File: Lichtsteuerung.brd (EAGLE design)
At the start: 157.7 x 86.4 mm, 155 parts, among them IC1 74HC595D, IC10 TSR_1-2450, IC11 MEGA64-A, IC12 75176AD, IC13 DS1307SO8, IC2 74HC595D, IC3 74HC595D, IC4 74HC595D, IC5 75176AD, IC6 MEGA8-AI, IC9 24FC128-I/SN, Q1 32.768, Q2 16MHz, Q3 16MHz, U1 MAX232SOIC16, X1 713-1410, X2 713-1410, X3 733-333, X5 713-1410, X6 733-334, X7 733-333, X8 733-333

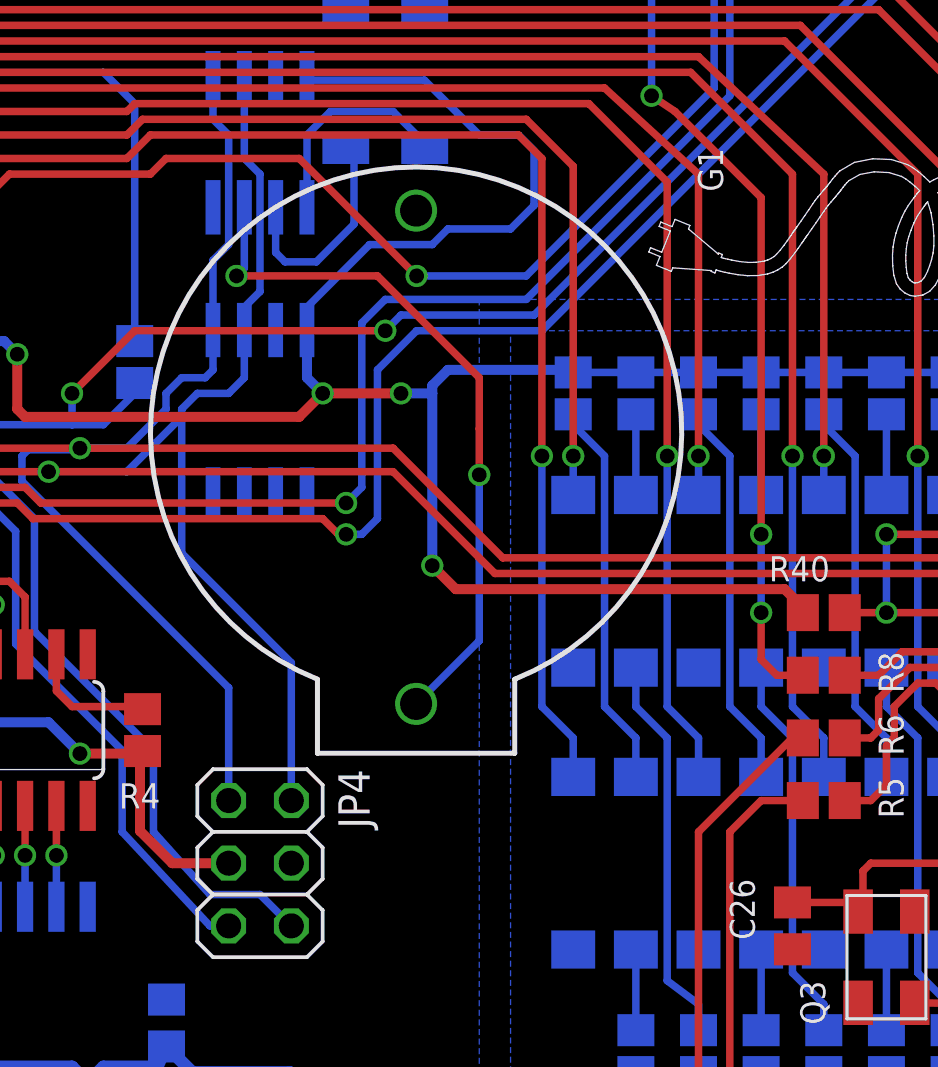
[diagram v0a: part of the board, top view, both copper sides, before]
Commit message: Changed CR2032 battery holder with a vertical one to allow easier replacements
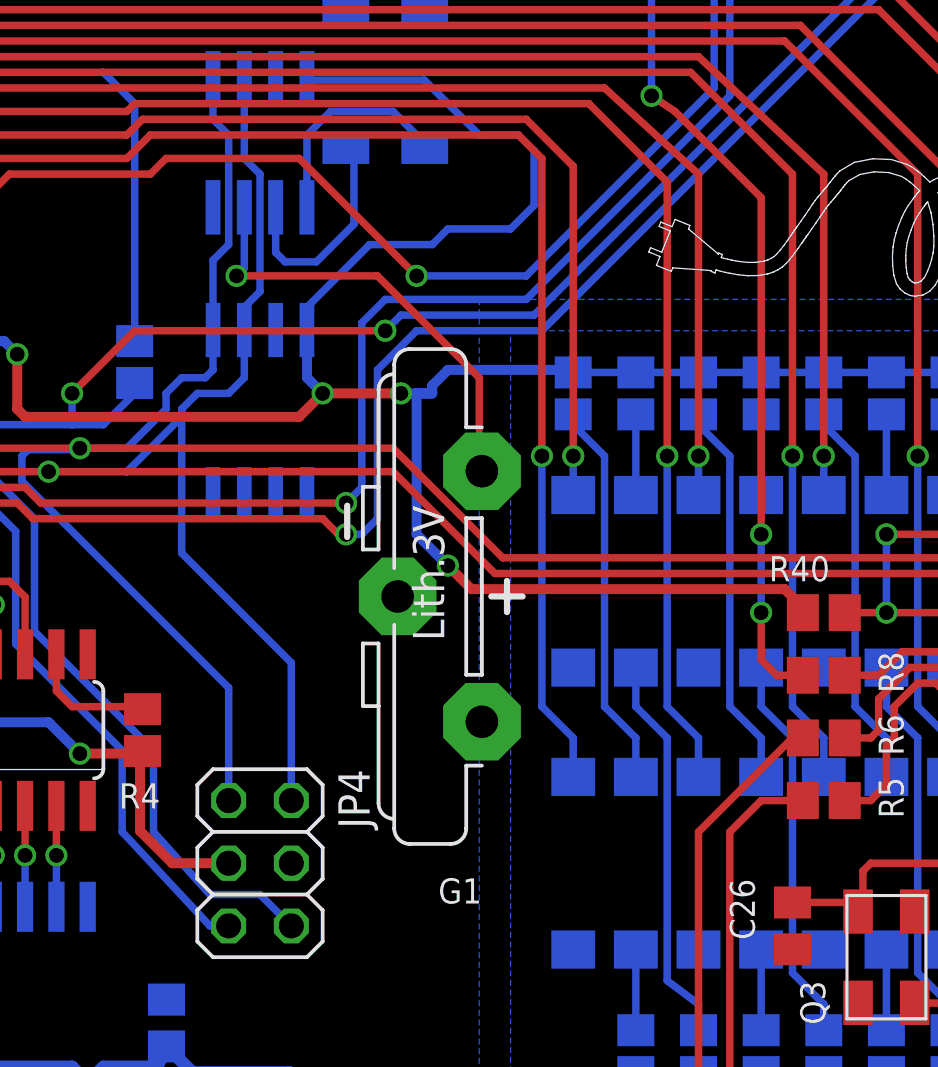
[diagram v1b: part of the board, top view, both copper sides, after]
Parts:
- G1: value (none) -> CR2032V; device SparkFun:BATTCOM_20MM_PTH -> cr2032v2:CR2032V2
- moved G1 15.6 mm to (104.2, 41.3), turned to 180 degrees
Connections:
- net GND: now also G1.-; no longer G1.2
- net N$40: now also G1.+; no longer G1.1
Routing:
- net N$40: track 28.8 -> 18.3 mm, vias 2 -> 1
- net +5V: track 543.3 -> 543.8 mm
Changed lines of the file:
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@@
 <setting verticaltext="up"/>
 </settings>
-<grid distance="50" unitdist="mil" unit="mil" style="lines" multiple="1" display="yes" altdistance="0.0125" altunitdist="inch" altunit="inch"/>
+<grid distance="0.000003125" unitdist="mm" unit="mm" style="lines" multiple="1" display="yes" altdistance="0.025" altunitdist="inch" altunit="inch"/>
 <layers>
 <layer number="1" name="Top" color="4" fill="1" visible="yes" active="yes"/>
@@
 <attribute name="NAME" x="95.25" y="61.2775" size="1.016" layer="26" rot="MR270"/>
 </element>
-<element name="G1" library="SparkFun" package="BATTCOM_20MM_PTH" value="" x="104.12" y="56.94" smashed="yes" rot="R270">
-<attribute name="NAME" x="115.55" y="59.48" size="1.016" layer="25" ratio="10" rot="R270"/>
+<element name="G1" library="cr2032v2" package="CR2032V2" value="CR2032V" x="104.2475" y="41.295" smashed="yes" rot="R180">
+<attribute name="NAME" x="106.7875" y="29.865" size="1.016" layer="25" ratio="10" rot="R180"/>
 </element>
 <element name="Q1" library="crystal" package="MC-306" value="32.768" x="102.87" y="62.23" smashed="yes" rot="MR90">
@@
 <contactref element="C9" pad="2"/>
 <contactref element="C10" pad="2"/>
-<contactref element="G1" pad="2"/>
+<contactref element="G1" pad="-"/>
 <contactref element="IC13" pad="4"/>
 <contactref element="C12" pad="2"/>
@@
 <wire x1="119.8" y1="40.64" x2="119.8" y2="40.855" width="0.4064" layer="1"/>
 <wire x1="119.8" y1="40.855" x2="119.0625" y2="41.5925" width="0.4064" layer="1"/>
-<wire x1="119.0625" y1="41.5925" x2="105.7275" y2="41.5925" width="0.4064" layer="1"/>
-<wire x1="105.7275" y1="41.5925" x2="104.775" y2="42.545" width="0.4064" layer="1"/>
-<via x="104.775" y="42.545" extent="1-16" drill="0.6"/>
-<wire x1="104.775" y1="42.545" x2="104.775" y2="49.53" width="0.4064" layer="16"/>
+<wire x1="119.0625" y1="41.5925" x2="106.3625" y2="41.5925" width="0.4064" layer="1"/>
+<wire x1="106.3625" y1="41.5925" x2="105.41" y2="42.545" width="0.4064" layer="1"/>
+<via x="105.41" y="42.545" extent="1-16" drill="0.6"/>
+<wire x1="105.41" y1="42.545" x2="104.14" y2="43.815" width="0.4064" layer="16"/>
+<wire x1="104.14" y1="43.815" x2="104.14" y2="49.53" width="0.4064" layer="16"/>
+<wire x1="104.14" y1="49.53" x2="104.775" y2="49.53" width="0.4064" layer="16"/>
 <wire x1="104.775" y1="49.53" x2="104.775" y2="49.8475" width="0.4064" layer="16"/>
 <wire x1="104.775" y1="49.8475" x2="105.41" y2="50.4825" width="0.4064" layer="16"/>
@@
 </signal>
 <signal name="N$40">
-<contactref element="G1" pad="1"/>
+<contactref element="G1" pad="+"/>
 <contactref element="IC13" pad="3"/>
 <wire x1="97.155" y1="57.0738" x2="97.155" y2="54.61" width="0.3048" layer="16"/>
@@
 <wire x1="102.5525" y1="54.2925" x2="106.68" y2="50.165" width="0.3048" layer="1"/>
 <wire x1="106.68" y1="50.165" x2="106.68" y2="48.095" width="0.3048" layer="1"/>
-<wire x1="106.68" y1="48.095" x2="106.68" y2="46.228" width="0.3048" layer="1"/>
-<via x="106.68" y="46.228" extent="1-16" drill="0.6" shape="square"/>
-<wire x1="106.68" y1="46.228" x2="106.68" y2="39.5" width="0.3048" layer="16"/>
-<wire x1="106.68" y1="39.5" x2="104.12" y2="36.94" width="0.3048" layer="16"/>
+<wire x1="106.68" y1="48.095" x2="106.68" y2="46.4825" width="0.254" layer="1"/>
+<wire x1="106.68" y1="46.4825" x2="106.7875" y2="46.375" width="0.254" layer="1"/>
 </signal>
 <signal name="SCL">

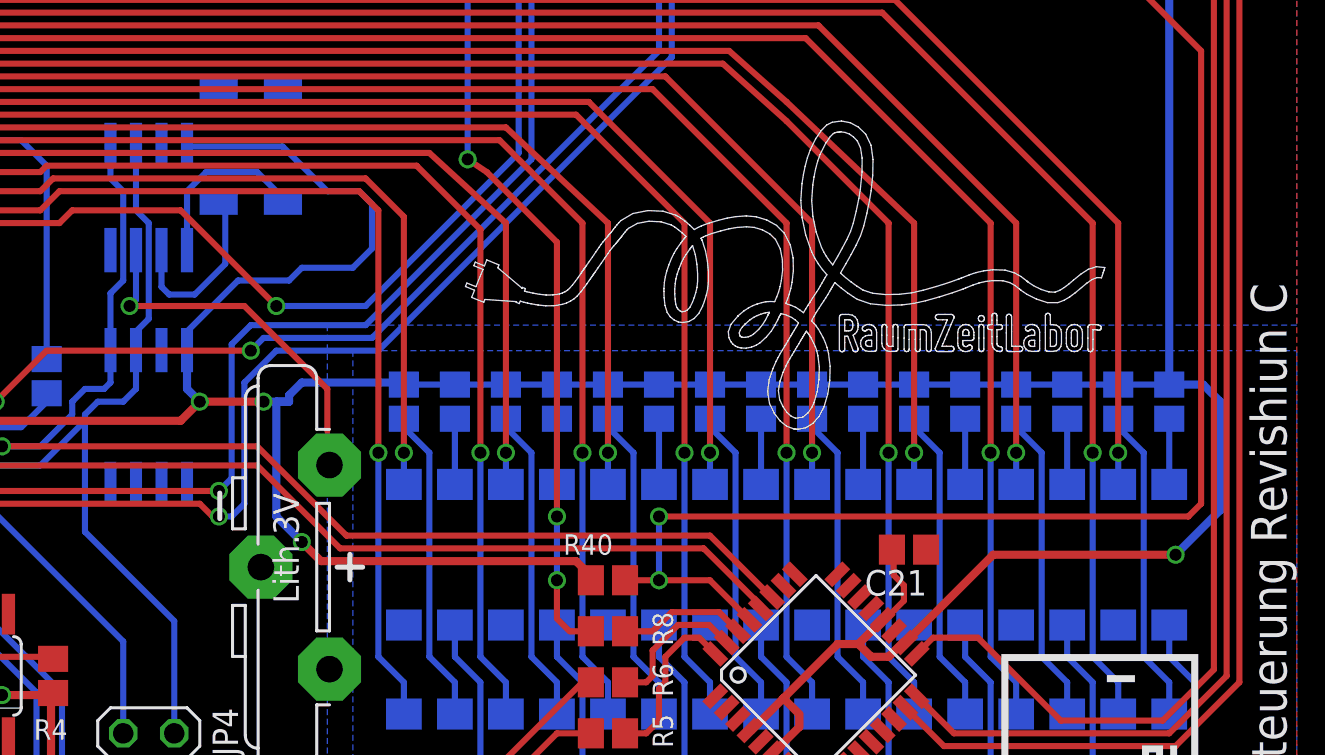
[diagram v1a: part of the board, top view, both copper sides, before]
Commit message: Added missing pulldowns for the optocoupler inputs
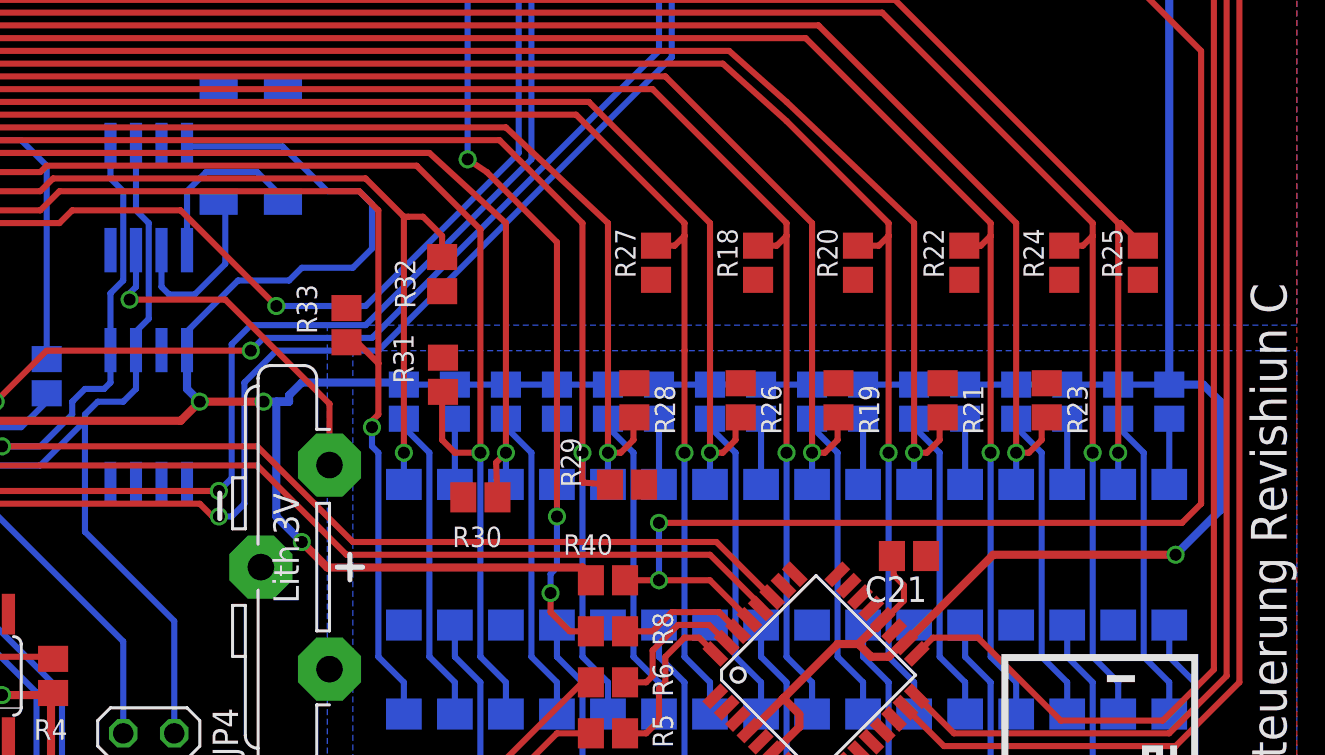
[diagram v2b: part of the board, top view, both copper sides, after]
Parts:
- removed U$1: (no value), RaumZeitLabor:RAUMZEITLABOR_-_LOGO_-_SCHWARZ
- added R18, R19, R20, R21, R22, R23, R24, R25, R26, R27, R28, R29, R30, R31, R32, R33: 10k, resistor:R0805
- moved C21 0.32 mm to (135.6, 41.8)
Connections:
- net GND: now also R18.1, R19.1, R20.1, R21.1, R22.1, R23.1, R24.1, R25.1, R26.1, R27.1, R28.1, R29.1, R30.1, R31.1, R32.1, R33.1
- net INPUT_1: now also R33.2
- net INPUT_10: now also R19.2
- net INPUT_11: now also R20.2
- net INPUT_12: now also R21.2
- net INPUT_13: now also R22.2
- net INPUT_14: now also R23.2
- net INPUT_15: now also R24.2
- net INPUT_16: now also R25.2
- net INPUT_2: now also R32.2
- net INPUT_3: now also R31.2
- net INPUT_4: now also R30.2
- net INPUT_5: now also R29.2
- net INPUT_6: now also R28.2
- net INPUT_7: now also R27.2
- net INPUT_8: now also R26.2
- net INPUT_9: now also R18.2
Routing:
- net INPUT_3: track 65.8 -> 70.4 mm
- net INPUT_2: track 49.9 -> 53.3 mm
- net INPUT_5: track 77.9 -> 80.8 mm
- net INPUT_8: track 79.5 -> 82.3 mm
- net INPUT_14: track 108.2 -> 111.0 mm
- net INPUT_12: track 106.1 -> 108.8 mm
- net INPUT_6: track 69.5 -> 72.2 mm
- net INPUT_10: track 105.2 -> 107.8 mm
- net INPUT_4: track 59.7 -> 62.2 mm
- net INPUT_1: track 60.2 -> 62.5 mm
- net INPUT_11: track 118.7 -> 120.4 mm
- net INPUT_16: track 110.2 -> 111.9 mm
- net INPUT_7: track 87.8 -> 89.4 mm
- net INPUT_15: track 122.4 -> 124.0 mm
- net INPUT_9: track 118.0 -> 119.7 mm
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
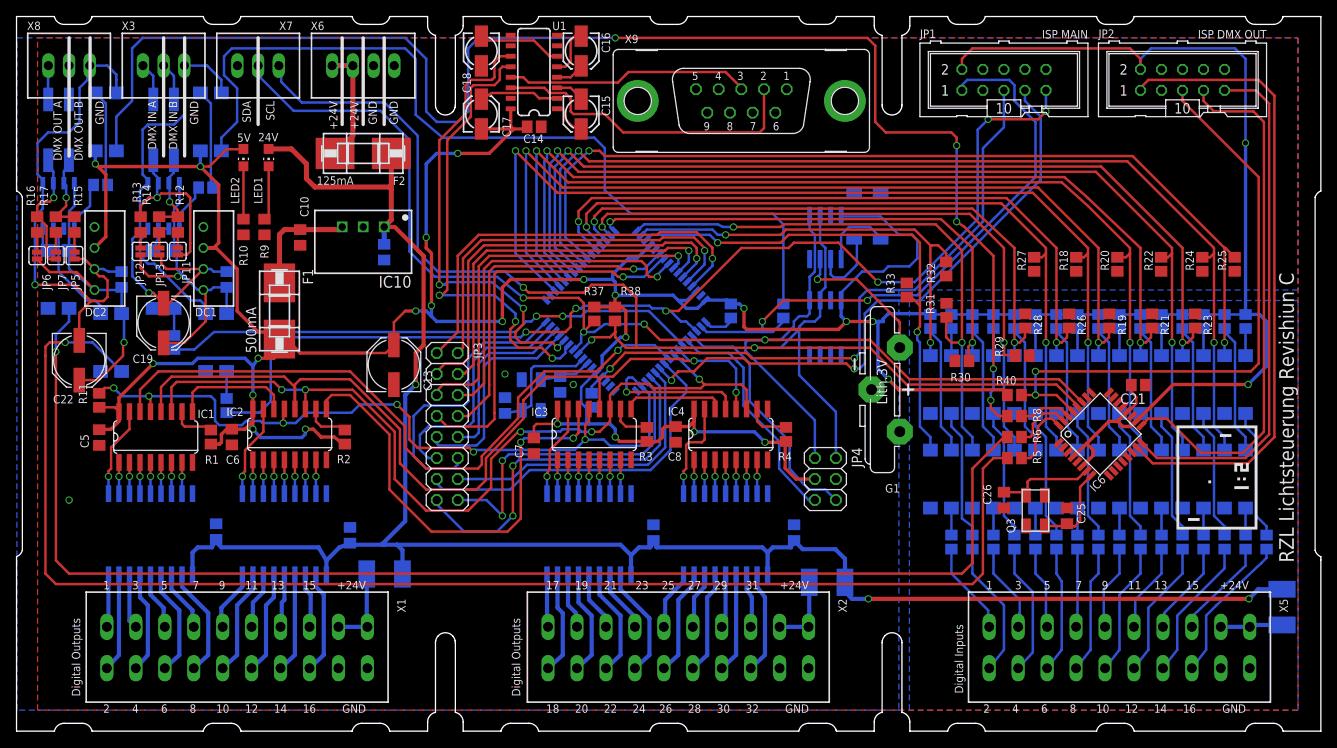
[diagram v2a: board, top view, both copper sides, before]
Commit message: Added new high-speed optocouplers
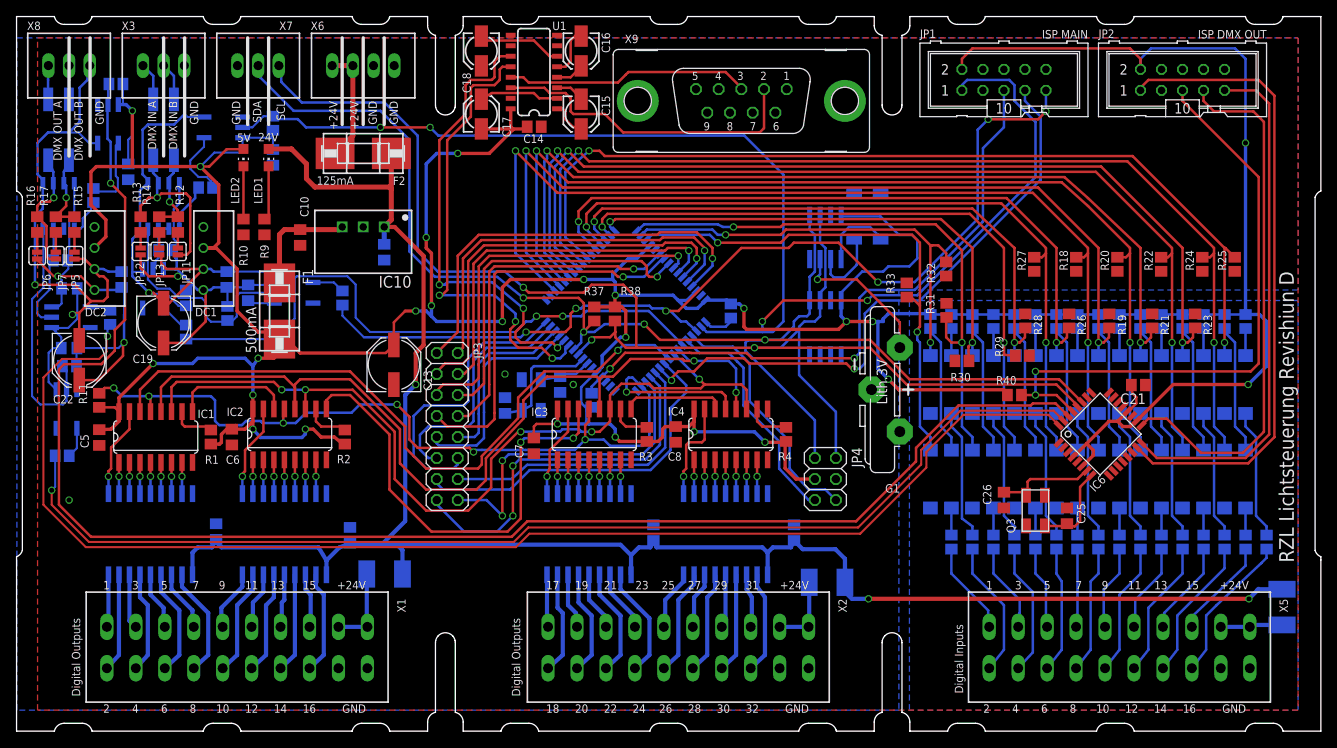
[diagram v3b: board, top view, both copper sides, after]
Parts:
- removed OK17, OK18, OK19, OK20, OK21, OK22: LTV356T, optocoupler:SMD4
- removed R5, R6: 220, resistor:R0805
- removed R76, R8: 10k, resistor:R0805
- added C24, C27, C28, C29, C30, C31: 100n, rcl:C0805
- added OK1, OK2, OK3, OK30, OK31, OK32: ACPL-M50L, ACPL-M50L:JEDEC_MS-012-AA_SOIC5
- added R34, R35, R36, R43, R44, R45: 1k, resistor:R0805
- added R41, R42: 220, resistor:R0805
- moved R74 19.1 mm to (39.4, 52.4)
- moved R7 16.0 mm to (11.3, 50.0), turned to 90 degrees
- moved R73 1.92 mm to (20.5, 48.2)
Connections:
- removed net N$106: OK17.3, R76.2
- removed net N$46: OK22.3, R8.2
- removed net N$47: OK20.1, R6.2
- removed net N$48: OK21.1, R5.2
- removed net REC$2: IC5.1, R7.2
- removed net RE_OUT1: IC5.2, IC5.3, OK21.3
- removed net TXD_OUT1: IC5.4, OK20.3
- new net N$73: OK2.1, R41.2
- new net N$79: OK1.1, R7.2
- new net REC$3: IC5.1, R42.2
- new net RE_OUT2: IC5.2, IC5.3, OK1.5, R43.1
- new net TXD_OUT2: IC5.4, OK2.5, R44.1
- net +5V: now also C30.1, C31.1, OK3.6, OK30.6, R36.1, R45.1; no longer OK17.4, OK22.4
- net DMX_O_D: now also R41.1; no longer R6.1
- net DMX_O_R: now also OK3.5, R45.2; no longer R8.1
- net GND: now also C30.2, C31.2, OK1.3, OK2.3, OK3.4, OK30.4, OK31.3, OK32.3; no longer OK18.2, OK19.2, OK20.2, OK21.2
- net GNDI1: now also C24.2, C27.2, OK30.3, OK31.4, OK32.4; no longer OK17.2
- net GNDI2: now also C28.2, C29.2, OK1.4, OK2.4, OK3.3; no longer OK22.2
- net N$104: now also OK30.1; no longer OK17.1
- net N$116: now also OK31.1; no longer OK18.1
- net N$133: now also OK32.1; no longer OK19.1
- net N$45: now also OK3.1, R42.1; no longer OK22.1, R7.1
- net RE/DE2: now also R7.1; no longer R5.1
- net RE_OUT: now also OK32.5, R34.1; no longer OK19.3
- net RXD/MOSI: now also OK30.5, R36.2; no longer R76.1
- net TXD_OUT: now also OK31.5, R35.1; no longer OK18.3
- net VCCIO1: now also C24.1, C27.1, OK31.6, OK32.6, R34.2, R35.2; no longer OK18.4, OK19.4
- net VCCIO2: now also C28.1, C29.1, OK1.6, OK2.6, R43.2, R44.2; no longer OK20.4, OK21.4
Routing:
- net DMX_O_R: track 6.55 -> 189.7 mm, vias 0 -> 1
- net N$46: track 177.6 -> 0.00 mm, vias 5 -> 0
- net N$48: track 168.9 -> 0.00 mm, vias 1 -> 0
- net N$47: track 160.7 -> 0.00 mm, vias 1 -> 0
- net RE/DE2: track 8.57 -> 160.9 mm, vias 0 -> 1
- net DMX_O_D: track 7.40 -> 138.4 mm, vias 0 -> 1
- net N$106: track 106.1 -> 0.00 mm
- net RXD/MOSI: track 72.4 -> 158.6 mm, vias 2 -> 4
- net TXD_OUT2: track 0.00 -> 30.0 mm
- net +5V: track 543.9 -> 572.2 mm
- net MISO: track 137.0 -> 117.7 mm
- net GNDI1: track 58.4 -> 76.5 mm
- net GNDI2: track 62.9 -> 79.1 mm, vias 1 -> 2
- net RE_OUT2: track 0.00 -> 14.5 mm
- net RE_OUT1: track 14.2 -> 0.00 mm
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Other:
- board text added: "RZL Lichtsteuerung Revishiun D"
- board text removed: "RZL Lichtsteuerung Revishiun C"
